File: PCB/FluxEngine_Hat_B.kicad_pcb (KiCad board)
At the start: 2 copper layers, 83.8 x 24.1 mm, 4 parts, among them J1 CY8CKIT-059, P1 FDD_IBMPC_host, P2 FDD_SA800_host

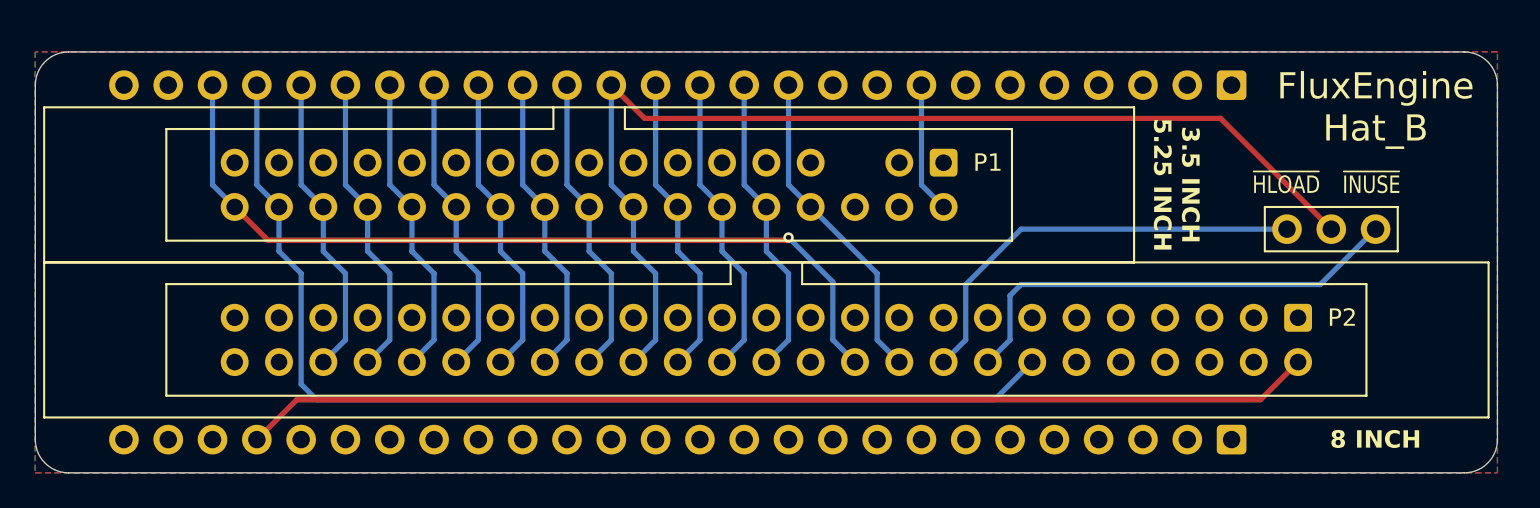
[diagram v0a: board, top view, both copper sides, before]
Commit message: snap cover, better 3d model files
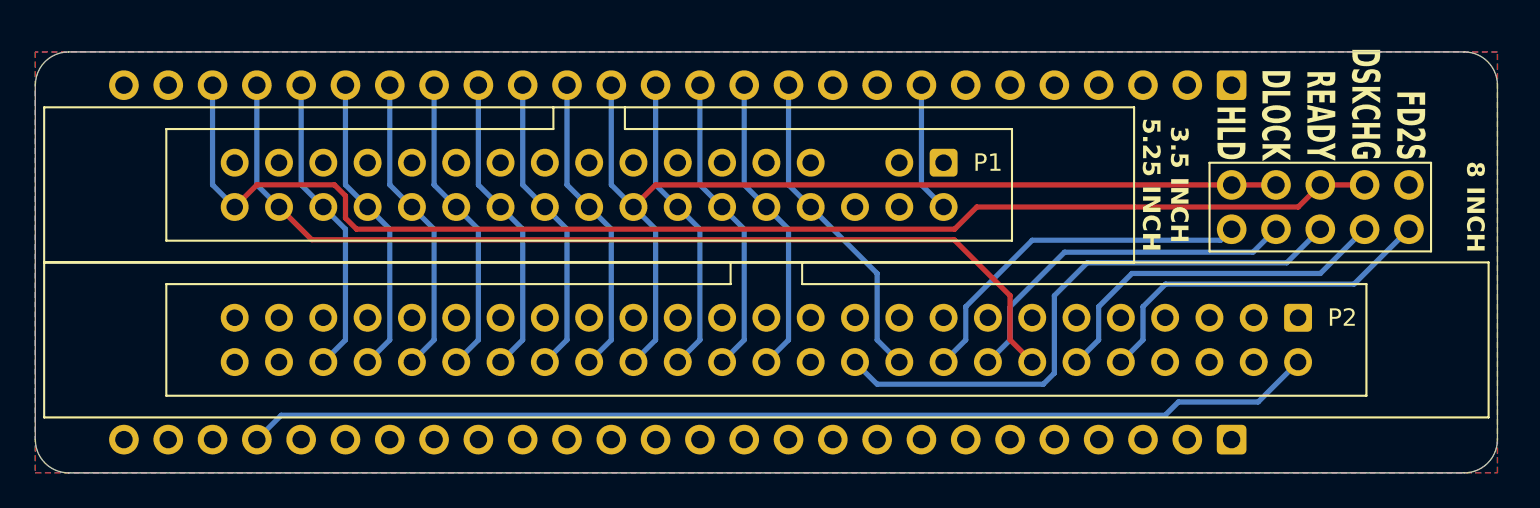
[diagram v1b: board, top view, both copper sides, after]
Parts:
- JP1: value Jumper_3_Open -> PinHeader_02x05; footprint 000_LOCAL:PinHeader_1x03_P2.54mm_Vertical bare -> 000_LOCAL:PinHeader_2x05_P2.54mm_Vertical
- moved JP1 8.25 mm to (171.5, 102.9), turned to 90 degrees
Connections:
- net /TK43 renamed /TG43
- JP1 pad 1: /~{INUSE} -> /~{HLD}
- JP1 pad 3: /~{HLOAD} -> /~{DLOCK}
- P2 pad 10: unconnected-(P2-~{FD2S}-Pad10) -> /~{FD2S}
- P2 pad 12: unconnected-(P2-DSKCHG-Pad12) -> /DC
- P2 pad 16: /~{INUSE} -> /~{DLOCK}
- P2 pad 18: /~{HLOAD} -> /~{HLD}
- P2 pad 22: /~{READY} -> /~{RDY}
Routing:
- net /~{RDY}: track 0.00 -> 33.5 mm
- net /~{INUSE}: track 26.9 -> 0.00 mm
- net /~{READY}: track 48.8 -> 75.7 mm, vias 1 -> 0
- net /~{HLOAD}: track 24.7 -> 0.00 mm
- net /~{FD2S}: track 0.00 -> 20.8 mm
- net /~{DLOCK}: track 0.00 -> 20.8 mm
- net /~{HLD}: track 0.00 -> 20.8 mm
- net /DC: track 0.00 -> 20.8 mm
- net /~{SEL4}: track 62.1 -> 54.8 mm
- net /SIDE: track 61.4 -> 55.9 mm
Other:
- board text added: "${COMMENT1} v${REVISION}"
- board text added: "${TITLE}"
- board text added: "FD2S DSKCHG READY DLOCK HLD"
- board text added: "button & usb face down towards connectors"
- board text removed: "${COMMENT1}"
- board text removed: "${TITLE} v${REVISION}"
- board text removed: "FluxEngine Hat_B"
- board text removed: "~{HLOAD}"
- board text removed: "~{INUSE}"
